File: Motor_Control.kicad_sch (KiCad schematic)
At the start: 36 parts, among them J15 Motor2 encoder, J16 MDD20A PWM2/DIR2/GND, J6 MDD20A PWM1/DIR1/GND, J7 Motor1 encoder, U10 74LVC2G17, U6 USBLC6-4SC6, U7 USBLC6-4SC6, U9 74LVC2G17

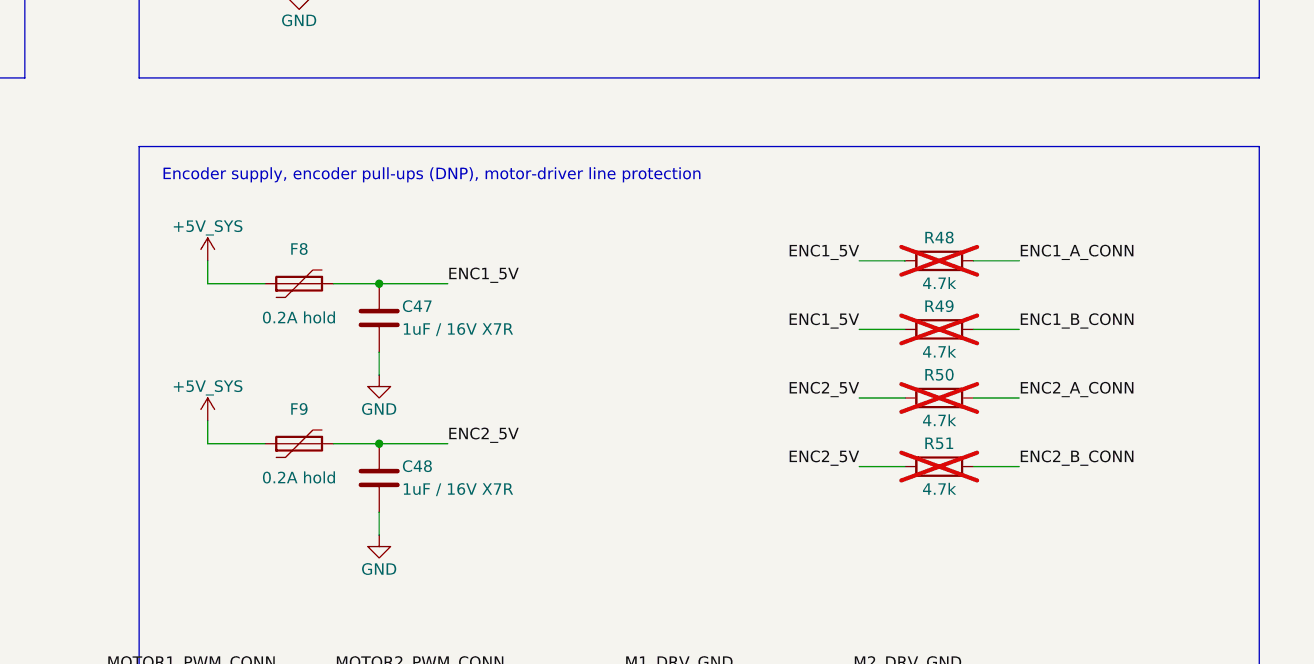
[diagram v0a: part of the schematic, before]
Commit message: Switch AUX ports to top-entry JST XH; drop encoder pull-ups and Pi sense
- J18-J21 (peripheral 5 V ports) are now top-entry JST XH B2B-XH-A:
  cables plug in from above, which suits a flat board you reach into,
  and the footprint drops from 107 to 58 mm2 per port. Use pre-made
  2-pin XH cables, so no crimping.
- Remove the DNP encoder pull-ups R48-R51. If the am-3651 outputs turn
  out to be open-collector, bodge 4.7k from each A/B line to ENCn_5V
  (noted on the Motor Control sheet).
- Remove the Pi-alive sense R44/R45. PA1 is a spare pin again (J8 pin
  2); the Pi's 3V3 on J13 still enables the AUX buck through D15.
- Board: same edits as Update PCB from Schematic (J18-J21 swapped,
  six resistors deleted, PA1 net restored on U1/J8); the parked parts
  are re-grouped beside the board. Venya's tracks unchanged (87).
- Docs, README and schematic PDF updated.

ERC 0/0. DRC: 0 errors, 3 existing text-size warnings, parity clean.
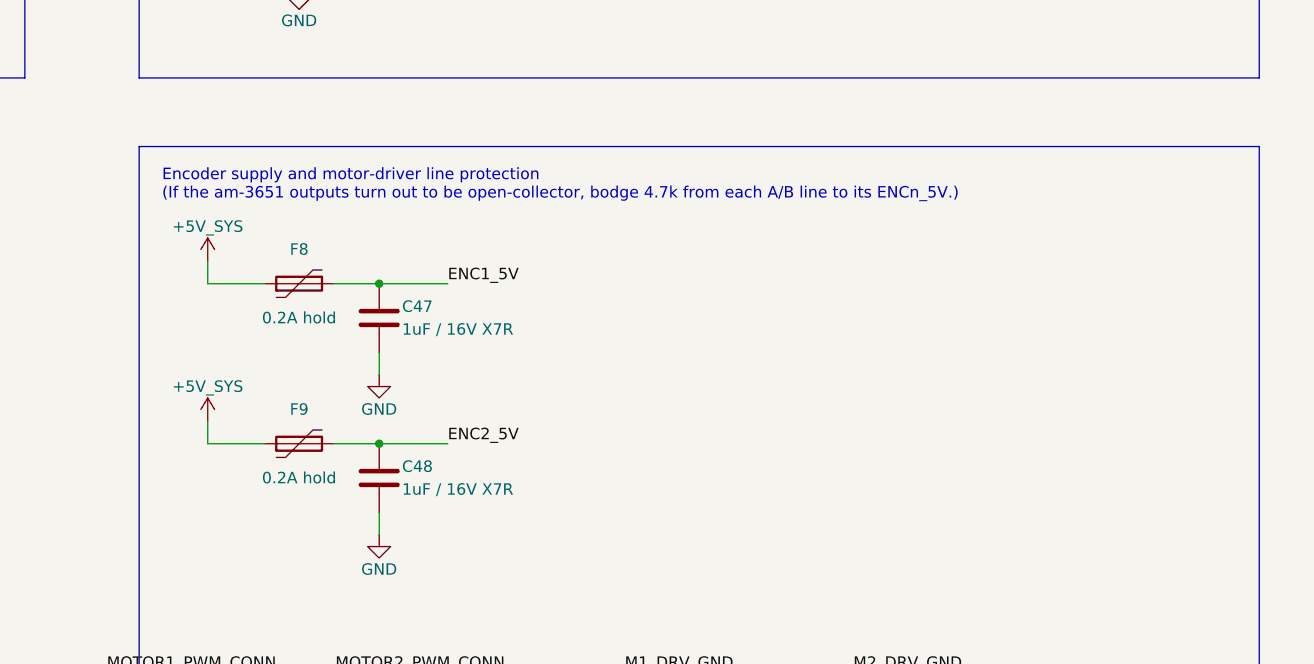
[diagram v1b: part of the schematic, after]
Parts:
- removed R48, R49, R50, R51: 4.7k, Resistor_SMD:R_0805_2012Metric, symbol Device:R
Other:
- note added: "Encoder supply and motor-driver line protection (If the am-3651 outputs turn out to be open-collector, bodge 4.7k from each A/B line to its ENCn_5V.)"
- note removed: "Encoder supply, encoder pull-ups (DNP), motor-driver line protection"

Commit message: Route the board and apply the prototype PCB checklist fixes
Routing
- Route power (pours, In2 power areas, vias) and all signals; add a
  Signal net class (0.15 mm width/clearance) for low-speed nets.
- J8 expansion header is now a 2x8 near the MCU.

Checklist red flags
- Crystal Y3 moved beside U1's OSC pins with C5/C6 outboard and no
  other signals under it.
- Vias untented by default (tented only under silkscreen); 15 mil
  test vias on key signals, recorded as DRC exclusions.
- ESD: U6/U7 split into four USBLC6-2SC6 (U6, U11, U7, U12), one per
  connector, with VBUS caps C50/C51; R12/R13 moved next to J13.
- GND test loop TP3 moved to the top edge beside J5.

Improvements
- Encoder connectors J7/J15 changed to keyed JST XH S4B side-entry.
- 43 passives/LEDs/FB2 moved from 0603 to 0805 (MPNs updated).
- Fifth M3 mounting hole H5 under J8.
- +3.3VA rerouted away from the crystal; acute track angles removed.
- Datasheet links filled in; silkscreen pin labels, pin maps, team
  names and date; reference labels cleared off pads and vias.
- Custom DRC rule for the J7/J15 silkscreen edge overhang.
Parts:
- added C50, C51: 100nF, Capacitor_SMD:C_0805_2012Metric, symbol Device:C
- added U11, U12: USBLC6-2SC6, Package_TO_SOT_SMD:SOT-23-6, symbol Power_Protection:USBLC6-2SC6
- C34, C35: footprint Capacitor_SMD:C_0603_1608Metric -> Capacitor_SMD:C_0805_2012Metric
- C41, C42: footprint Capacitor_SMD:C_0603_1608Metric -> Capacitor_SMD:C_0805_2012Metric; MPN C0603C104K5RACTU -> C0805C104K5RACTU
- C43, C44, C45, C46: footprint Capacitor_SMD:C_0603_1608Metric -> Capacitor_SMD:C_0805_2012Metric; MPN GRM1885C1H102JA01D -> C0805C102J5GACTU; Manufacturer Murata -> KEMET
- C47, C48: footprint Capacitor_SMD:C_0603_1608Metric -> Capacitor_SMD:C_0805_2012Metric; MPN C1608X7R1C105K080AC -> GRM21BR71C105KA01L; Manufacturer TDK -> Murata
- J15, J7: footprint TerminalBlock_Phoenix:TerminalBlock_Phoenix_MKDS-1,5-4_1x04_P5.00mm_Horizontal -> Connector_JST:JST_XH_S4B-XH-A_1x04_P2.50mm_Horizontal; symbol Connector:Screw_Terminal_01x04 -> Connector_Generic:Conn_01x04; MPN 1715048 (MKDS 1,5/4, 5.0 mm pitch) -> S4B-XH-A(LF)(SN); Manufacturer Phoenix Contact -> JST; Rating 17.5 A / 250 V (IEC), 26-14 AWG; this design: 5 V, 2 A max 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 -> 3 A per contact
- U6, U7: value USBLC6-4SC6 -> USBLC6-2SC6; symbol Power_Protection:USBLC6-4SC6 -> Power_Protection:USBLC6-2SC6; MPN USBLC6-4SC6 -> USBLC6-2SC6
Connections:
- net +3V3: now also C50.1, U11.5 (VBUS)
- net +5V_SYS: now also C51.1, U12.5 (VBUS)
- net ENC1_A_CONN: now also U7.6 (I/O1)
- net ENC1_B_CONN: now also U7.4 (I/O2)
- net ENC2_A_CONN: now also U12.1 (I/O1), U12.6 (I/O1); no longer U7.4 (I/O3)
- net ENC2_B_CONN: now also U12.3 (I/O2), U12.4 (I/O2); no longer U7.6 (I/O4)
- net GND: now also C50.2, C51.2, U11.2 (GND), U12.2 (GND)
- net MOTOR1_DIR_CONN: now also U6.4 (I/O2)
- net MOTOR1_PWM_CONN: now also U6.6 (I/O1)
- net MOTOR2_DIR_CONN: now also U11.3 (I/O2), U11.4 (I/O2); no longer U6.6 (I/O4)
- net MOTOR2_PWM_CONN: now also U11.1 (I/O1), U11.6 (I/O1); no longer U6.4 (I/O3)
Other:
- note added: "ESD arrays - one per connector: U6 J6, U11 J16, U7 J7, U12 J15"
- note removed: "ESD arrays - U6: J6 + J16, U7: J7 + J15"
- moved on the sheet: C34, C35
